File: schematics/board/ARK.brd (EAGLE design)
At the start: 89 x 89 mm, 213 parts, among them IC2 STM32F103C8T, Q5 8MHz

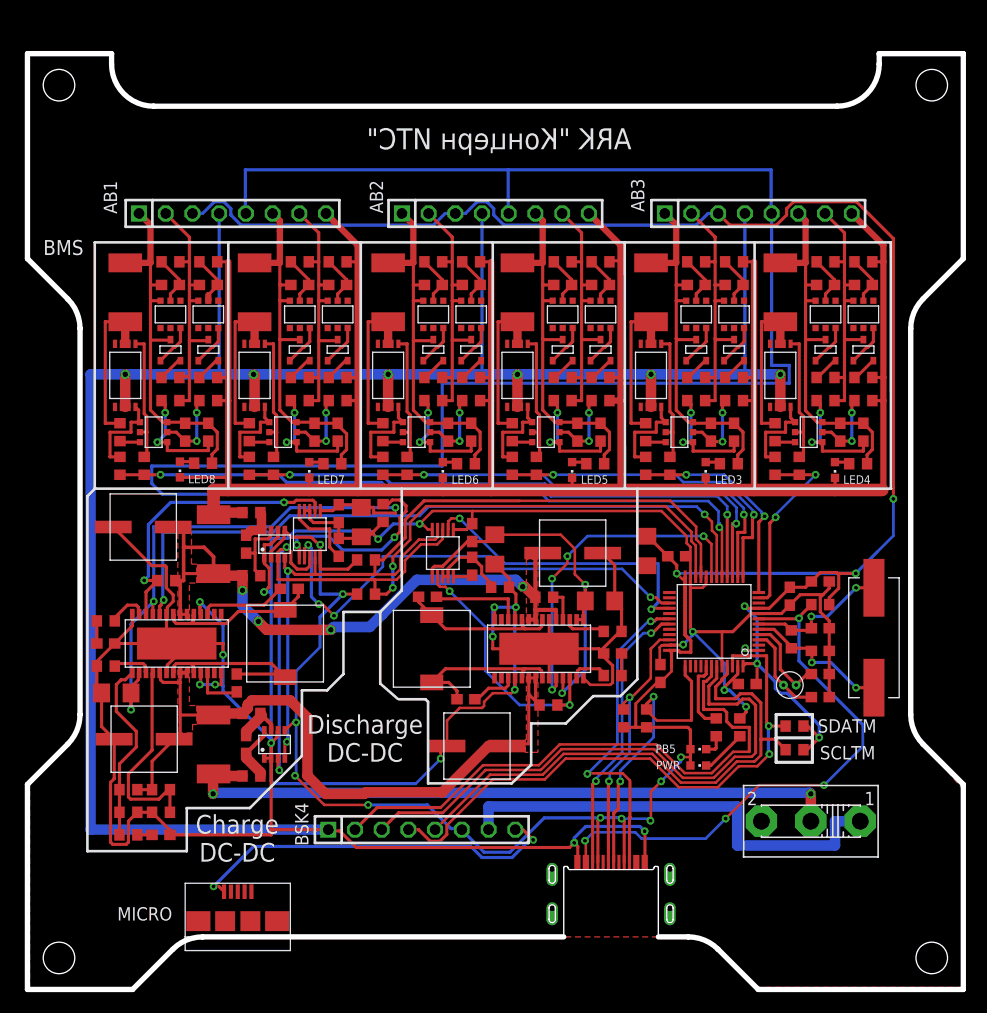
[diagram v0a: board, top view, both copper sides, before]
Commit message: Обновлен список плат, работа над платой ПН
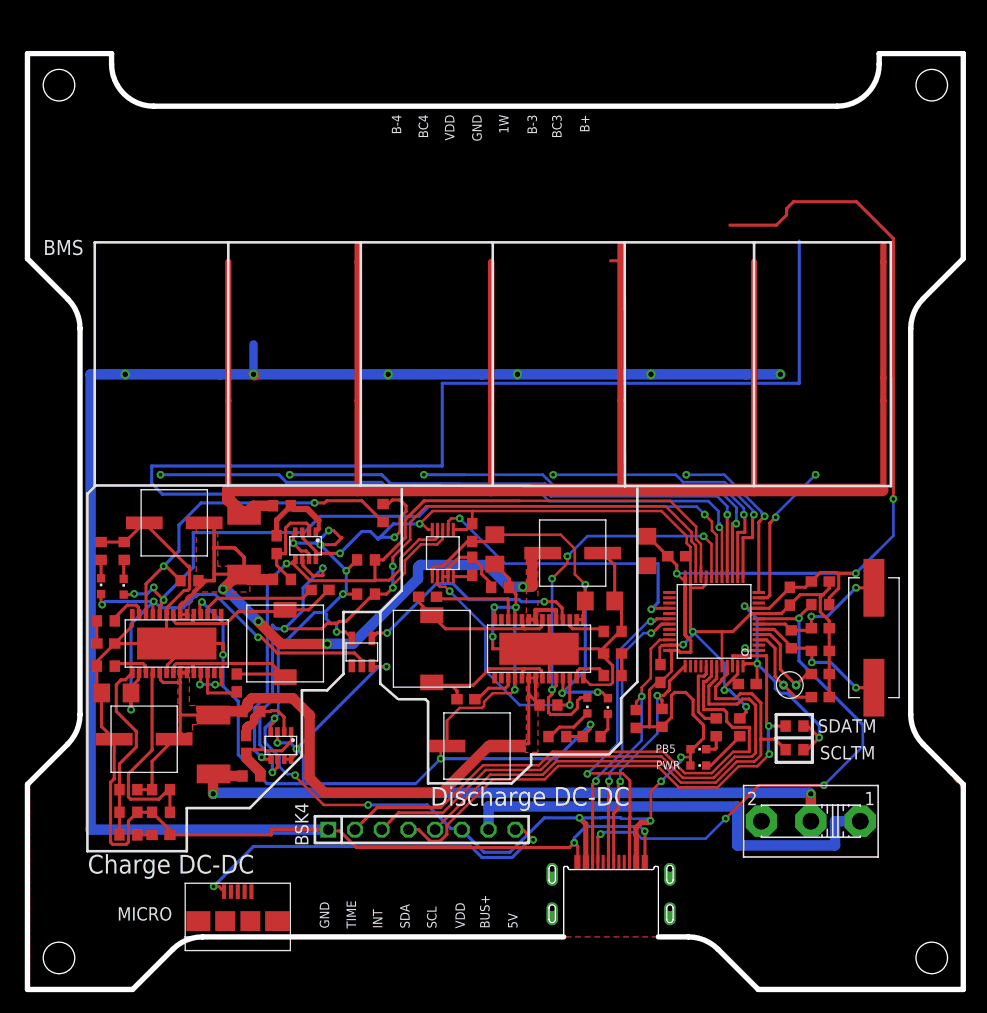
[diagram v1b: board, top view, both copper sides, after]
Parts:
- removed AB1, AB2, AB3: (no value), pinheadCS:1X08
- removed C1, C10, C11, C12, C17, C18, C19, C2, C20, C21, C22, C23, C24, C25, C26, C27, C28, C3, C32, C4, C5, C6, C7, C8, C9: 0,1µ, rcl:C0603
- removed C42: 1µ, rcl:C0603
- removed C43: 10µ, rcl:C1206
- removed LED4, LED5, LED6, LED7: (no value), led:CHIPLED_0603
- removed R1, R17, R33, R41, R49, R80, R83, R84, R85, R86, R9: 2k, resistor:R0603
- removed R10, R11, R18, R19, R2, R3, R34, R35, R42, R43, R50, R51: 330R, resistor:R0603
- removed R12, R13, R14, R15, R20, R21, R22, R23, R36, R37, R38, R39, R4, R44, R45, R46, R47, R5, R52, R53, R54, R55, R6, R7, R88, R89, R90, R91, R92, R93, R94, R95, R96, R97, R98, R99: 100R, resistor:R0603
- removed R16, R24, R40, R48, R56, R8: R05, rcl:R2512
- removed R63: 1M, resistor:R0603
- removed U$1, U$15, U$24, U$25, U$26, U$8: FS8205A-, CanCubeSat:FS8205A-
- removed U$10, U$17, U$3, U$31, U$38, U$45: HY2120, CanCubeSat:HY2120
- removed U$11, U$12, U$18, U$19, U$32, U$33, U$39, U$4, U$40, U$46, U$47, U$5: HY2213, CanCubeSat:HY2213
- removed U$13, U$14, U$20, U$21, U$34, U$35, U$41, U$42, U$48, U$49, U$6, U$7: SI2302CDS, CanCubeSat:SI2302CDS
- removed U$60: AD5272, CanCubeSat:AD5272
- added LED1, LED2: (no value), led:CHIPLED_0603
- added R31, R32, R57: 2k, resistor:R0603
- added U$2: INVERTER, CanCubeSat:INVERTER
- R70: value 14k3 -> 24k3
- R72: value 91k -> 232k
- moved LED3 25.1 mm to (53.2, 27.0)
- moved LED8 13.4 mm to (7.00, 38.4), turned to 0 degrees
- moved R100 12.8 mm to (7.00, 41.7), turned to 270 degrees
- moved C35 2.98 mm to (14.0, 44.4)
- moved R76 2.97 mm to (24.2, 46.0)
- moved U$57 2.95 mm to (26.4, 42.2), turned to 270 degrees
- moved C34 2.92 mm to (27.8, 38.0)
- moved R77 2.92 mm to (24.2, 39.0)
- moved R75 2.90 mm to (20.6, 42.3)
- moved C41 2.90 mm to (23.7, 42.3)
- moved R72 2.20 mm to (15.4, 38.9)
- moved R27 1.45 mm to (60.4, 25.8)
- moved R64 1.20 mm to (57.9, 25.7)
- moved INA219#1 0.61 mm to (24.1, 23.2), turned to 270 degrees
- moved R74 0.20 mm to (21.3, 26.4)
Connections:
- removed net B-1: AB1.6, C1.2, C2.2, C4.2, R8.2, R86.1, U$3.6, U$5.3, U$7.3
- removed net B-2: AB1.1, C25.2, C26.2, C28.2, R100.1, R56.2, U$45.6, U$47.3, U$49.3
- removed net B-3: AB2.6, C5.2, C6.2, C8.2, R16.2, R84.1, U$10.6, U$12.3, U$14.3
- removed net B-4: AB2.1, C21.2, C22.2, C24.2, R48.2, R85.1, U$38.6, U$40.3, U$42.3
- removed net B-5: AB3.6, C10.2, C12.2, C9.2, R24.2, R83.1, U$17.6, U$19.3, U$21.3
- removed net B-6: AB3.1, C17.2, C18.2, C20.2, R40.2, R80.1, U$31.6, U$33.3, U$35.3
- removed net DPC_RST: IC2.27, U$60.7
- removed net N$1: C1.1, R2.1, U$3.5
- removed net N$10: R5.1, U$7.2
- removed net N$100: U$46.6, U$48.1
- removed net N$101: R52.1, U$48.2
- removed net N$102: U$47.6, U$49.1
- removed net N$103: R53.1, U$49.2
- removed net N$104: R49.2, R56.1, U$1.67
- removed net N$107: C26.1, R51.1, U$45.4
- removed net N$108: C28.1, R55.1, U$47.2
- removed net N$110: AB1.2, C27.2, R51.2, R53.2, R55.2, U$46.3, U$48.3
- removed net N$13: R1.2, R8.1, U$26.67
- removed net N$141: C40.2, INA219#1.7, R74.2
- removed net N$15: C2.1, R3.1, U$3.4
- removed net N$154: C42.1, U$60.5
- removed net N$16: C5.1, R10.1, U$10.5
- removed net N$18: R9.1, U$10.3
- removed net N$19: C7.1, R14.1, U$11.2
- removed net N$2: C4.1, R7.1, U$5.2
- removed net N$20: U$11.6, U$13.1
- removed net N$21: R12.1, U$13.2
- removed net N$22: U$12.6, U$14.1
- removed net N$23: R13.1, U$14.2
- removed net N$24: R16.1, R9.2, U$25.67
- removed net N$27: C6.1, R11.1, U$10.4
- removed net N$28: C8.1, R15.1, U$12.2
- removed net N$3: R1.1, U$3.3
- removed net N$30: AB2.7, C7.2, R11.2, R13.2, R15.2, U$11.3, U$13.3
- removed net N$33: C9.1, R18.1, U$17.5
- removed net N$34: R17.1, U$17.3
- removed net N$35: C11.1, R22.1, U$18.2
- removed net N$36: U$18.6, U$20.1
- removed net N$37: R20.1, U$20.2
- removed net N$38: U$19.6, U$21.1
- removed net N$39: R21.1, U$21.2
- removed net N$4: C3.1, R6.1, U$4.2
- removed net N$40: R17.2, R24.1, U$24.67
- removed net N$43: C10.1, R19.1, U$17.4
- removed net N$44: C12.1, R23.1, U$19.2
- removed net N$45: C32.1, C39.1, C43.1, U$59.11, U$59.16, U$60.1
- removed net N$46: AB3.7, C11.2, R19.2, R21.2, R23.2, U$18.3, U$20.3
- removed net N$53: R63.1, U$16.18
- removed net N$57: LED5.A, R84.2
- removed net N$58: LED6.A, R85.2
- removed net N$59: LED7.A, R86.2
- removed net N$6: U$4.6, U$6.1
- removed net N$65: C17.1, R34.1, U$31.5
- removed net N$66: R33.1, U$31.3
- removed net N$67: C19.1, R38.1, U$32.2
- removed net N$68: U$32.6, U$34.1
- removed net N$69: R36.1, U$34.2
- removed net N$7: R4.1, U$6.2
- removed net N$70: U$33.6, U$35.1
- removed net N$71: R37.1, U$35.2
- removed net N$72: R33.2, R40.1, U$15.67
- removed net N$75: C18.1, R35.1, U$31.4
- removed net N$76: C20.1, R39.1, U$33.2
- removed net N$78: AB3.2, C19.2, R35.2, R37.2, R39.2, U$32.3, U$34.3
- removed net N$8: AB1.7, C3.2, R3.2, R5.2, R7.2, U$4.3, U$6.3
- removed net N$81: C21.1, R42.1, U$38.5
- removed net N$82: R41.1, U$38.3
- removed net N$83: C23.1, R46.1, U$39.2
- removed net N$84: U$39.6, U$41.1
- removed net N$85: R44.1, U$41.2
- removed net N$86: U$40.6, U$42.1
- removed net N$87: R45.1, U$42.2
- removed net N$88: R41.2, R48.1, U$8.67
- removed net N$9: U$5.6, U$7.1
- removed net N$91: C22.1, R43.1, U$38.4
- removed net N$92: C24.1, R47.1, U$40.2
- removed net N$94: AB2.2, C23.2, R43.2, R45.2, R47.2, U$39.3, U$41.3
- removed net N$97: C25.1, R50.1, U$45.5
- removed net N$98: R49.1, U$45.3
- removed net N$99: C27.1, R54.1, U$46.2
- removed net OC1: R95.2, U$26.5, U$3.2
- removed net OC2: R99.2, U$1.5, U$45.2
- removed net OC3: R93.2, U$10.2, U$25.5
- removed net OC4: R97.2, U$38.2, U$8.5
- removed net OC5: R91.2, U$17.2, U$24.5
- removed net OC6: R89.2, U$15.5, U$31.2
- removed net OD1: R94.2, U$26.4, U$3.1
- removed net OD2: R98.2, U$1.4, U$45.1
- removed net OD3: R92.2, U$10.1, U$25.4
- removed net OD4: R96.2, U$38.1, U$8.4
- removed net OD5: R90.2, U$17.1, U$24.4
- removed net OD6: R88.2, U$15.4, U$31.1
- new net A: C39.1, LED8.A, U$2.P$2, U$59.11, U$59.16
- new net N$14: C40.2, INA219#1.2, R74.2
- new net Y: U$16.18, U$2.P$4
- net 1W: no longer AB1.5, AB2.5, AB3.5
- net BMS+: no longer AB1.8, AB2.8, AB3.8, LED3.C, LED4.C, LED5.C, LED6.C, LED7.C, LED8.C, R10.2, R12.2, R14.2, R18.2, R2.2, R20.2, R22.2, R34.2, R36.2, R38.2, R4.2, R42.2, R44.2, R46.2, R50.2, R52.2, R54.2, R6.2
- net BMS1: no longer R94.1, R95.1
- net BMS2: no longer R98.1, R99.1
- net BMS3: no longer R92.1, R93.1
- net BMS4: no longer R96.1, R97.1
- net BMS5: no longer R90.1, R91.1
- net BMS6: no longer R88.1, R89.1
- net GND: now also INA219#1.3, INA219#1.7, INA219#1.8, R100.1, R31.1, R32.1, R57.1, R70.2, U$2.P$3, U$57.3, U$57.8; no longer AB1.4, AB2.4, AB3.4, C32.2, C42.2, C43.2, INA219#1.1, INA219#1.2, INA219#1.6, R70.1, U$1.23, U$15.23, U$24.23, U$25.23, U$26.23, U$57.1, U$57.6, U$60.3, U$60.4, U$8.23
- net INA_BMS+: no longer R63.2
- net N$147: now also INA219#1.1; no longer INA219#1.8
- net N$150: now also U$57.1; no longer U$57.8
- net N$151: now also U$57.2; no longer U$57.7
- net N$25: now also R70.1; no longer U$60.2
- net N$26: now also LED1.C, R31.2; no longer R70.2, U$60.6
- net N$47: now also LED1.A
- net N$54: now also LED2.C, R32.2; no longer LED3.A, R80.2
- net N$56: now also LED3.C, R57.2; no longer LED4.A, R83.2
- net N$60: now also LED8.C; no longer LED8.A
- net PGOOD1: now also LED2.A
- net PGOOD2: now also LED3.A
- net SCL: now also INA219#1.5, U$57.5; no longer INA219#1.4, U$57.4, U$60.9
- net SDA: now also INA219#1.6, U$57.6; no longer INA219#1.3, U$57.3, U$60.8
- net VDD: now also INA219#1.4, U$2.P$5, U$57.4, U$57.7; no longer AB1.3, AB2.3, AB3.3, INA219#1.5, U$57.2, U$57.5, U$60.10
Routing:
- net 1W: track 211.9 -> 146.0 mm
- net GND: track 579.7 -> 520.3 mm, vias 25 -> 28
- net N$45: track 55.7 -> 0.00 mm, vias 3 -> 0
- net A: track 0.00 -> 46.0 mm, vias 0 -> 4
- net DPC_RST: track 46.0 -> 0.00 mm, vias 4 -> 0
- net VDD: track 303.0 -> 259.4 mm, vias 17 -> 20
- net BMS+: track 245.9 -> 204.3 mm
- net B-6: track 36.0 -> 0.00 mm
- net B-4: track 35.9 -> 0.00 mm
- net B-2: track 35.8 -> 0.00 mm
- net B-5: track 35.8 -> 0.00 mm
- net B-3: track 35.8 -> 0.00 mm
- net B-1: track 35.7 -> 0.00 mm
- net N$110: track 25.3 -> 0.00 mm
- net N$78: track 25.2 -> 0.00 mm
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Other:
- board text added: "1W"
- board text added: "5V"
- board text added: "B+"
- board text added: "B-3"
- board text added: "B-4"
- board text added: "BC3"
- board text added: "BC4"
- board text added: "BUS+"
- board text added: "GND"
- board text added: "INT"
- board text added: "SCL"
- board text added: "SDA"
- board text added: "TIME"
- board text added: "VDD"

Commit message: Добавлены герберы плат BSK1-4, PL, SP и SPIDER
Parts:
- removed BSK4: (no value), pinheadCS:1X08
- removed C005R: 32,768KHz, CanCubeSat:C005R
- removed C13, C14, C33, C34, C51: 0,1µ, rcl:C0603
- removed C30, C36: 680p, rcl:C0603
- removed C31, C39: 4.7µ, rcl:C1206
- removed C35: 150µ, CanCubeSat:ECAP150
- removed C37: 220µ, CanCubeSat:ECAP220
- removed C38: 3,3n, rcl:C0603
- removed LED1, LED2, LED3, LED8: (no value), led:CHIPLED_0603
- removed MICRO: 629105136821, MicroUSB:629105136821
- removed Q5: 8MHz, 9C-8.000MEEJ-T:XTAL_9C-8.000MEEJ-T
- removed R25, R26: 5k1, resistor:R0603
- removed R29: 150k, resistor:R0603
- removed R31: 2k, resistor:R0603
- removed R61: 91K, resistor:R0603
- removed R62, R72: 232k, resistor:R0603
- removed R70: 24k3, resistor:R0603
- removed R78: 1M, resistor:R0603
- removed R87: 680k, resistor:R0603
- removed S1: (no value), cansat-lib:UNICS-SWITCH
- removed U$16: LTC3119, CanCubeSat:LTC3119
- added C1: 1nF, rcl:C0603
- added C10, C56, C9: 0,1µ, rcl:C0603
- added C2: 10nF, rcl:C0603
- added C3, C57: 10µ, rcl:C1206
- added C4, C5, C6, C7, C8: 100nF, rcl:C0603
- added CAM1, CAM2, SWITCH: (no value), pinheadCS:1X02
- added INVERT: INVERTER., CanCubeSat:SC70
- added JP1: (no value), pinheadCS:2X08
- added LD1117S33: LD1117S33, CanCubeSat:SOT223
- added LED_G1, LED_G2, LED_R1, LED_R2: (no value), led:CHIPLED_0603
- added OPA: OPA333, CanCubeSat:SOT23-5
- added R1: 91K, resistor:R0603
- added R2: 3313J-1-205E, CanCubeSat:TRIM_3313J-1-205E
- added R3: 14K3, resistor:R0603
- added R33: 2k, resistor:R0603
- added R4, R5, R6: 3314G-1-504E, CanCubeSat:TRIM_3314G-1-504E
- added U$1: MF-R400, CanCubeSat:MF-R400
- added U$12: FFC-CONNECT68611, CanCubeSat:68611
- 3,3µH1: value 3,3µ -> 3,3µH
- AD5272#2: device CanCubeSat:AD5272 -> CanCubeSat:MSOP10
- C44: value 27pF -> 680p
- C45: value 27pF -> 4.7µ; device rcl:C0603 -> rcl:C1206
- C46: value 10pF -> 3,3n
- C47: value 10pF -> 150µ; device rcl:C0603 -> CanCubeSat:ECAP150-CMD
- C48, C55: value 100nF -> 220µ; device rcl:C0603 -> CanCubeSat:ECAP220-CMD
- C49: value 150µ -> 0,1µ; device CanCubeSat:ECAP150 -> rcl:C0603
- C50: value 220µ -> 0,1µ; device CanCubeSat:ECAP220 -> rcl:C0603
- C52: value 10µ -> 680p; device rcl:C1206 -> rcl:C0603
- C53: value 100nF -> 4.7µ; device rcl:C0603 -> rcl:C1206
- C54: value 100nF -> 150µ; device rcl:C0603 -> CanCubeSat:ECAP150-CMD
- INA219#1, U$57: device CanCubeSat:INA219AID -> CanCubeSat:SOT23-8
- R30: value 14K3 -> 150k
- U$2: value INVERTER -> Q24; device CanCubeSat:INVERTER -> CanCubeSat:Q24
- U$23: value USB-C -> LTC31191; device CanCubeSat:USB-C -> CanCubeSat:LTC3119+VIA
- U$59: value LTC3119 -> LTC31191; device CanCubeSat:LTC3119 -> CanCubeSat:LTC3119+VIA
- moved C53 64.4 mm to (16.4, 67.0)
- moved R71 63.5 mm to (59.3, 71.3)
- moved C47 60.0 mm to (15.9, 22.5)
- moved R73 59.5 mm to (55.5, 69.0), turned to 180 degrees
- moved C44 59.2 mm to (20.4, 12.5)
- moved R74 58.2 mm to (55.5, 73.6)
- moved U$23 58.1 mm to (24.4, 54.1), turned to 90 degrees
- moved INA219#1 53.4 mm to (50.6, 69.6), turned to 180 degrees
- moved C46 52.6 mm to (24.4, 15.0)
- moved C55 51.6 mm to (15.9, 56.5), turned to 180 degrees
- moved R28 50.2 mm to (15.4, 64.0), turned to 0 degrees
- moved R57 48.8 mm to (7.30, 46.9)
- moved C45 47.5 mm to (32.4, 12.0)
- moved C48 45.5 mm to (32.9, 22.5)
- moved C54 44.0 mm to (32.9, 56.5), turned to 180 degrees
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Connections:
- removed net I2CINT: BSK4.3, IC2.43
- removed net N$11: 3,3µH1.2, C13.1, U$16.21, U$16.24
- removed net N$12: 3,3µH1.1, C14.1, U$16.5, U$16.8
- removed net N$133: C44.1, IC2.6, Q5.1, R78.1
- removed net N$145: C45.1, IC2.5, Q5.2, R78.2
- removed net N$148: C005R.P$2, C47.1, IC2.4
- removed net N$152: C005R.P$1, C46.1, IC2.3
- removed net N$25: R70.1, R72.1, U$59.12
- removed net N$26: LED1.C, R31.2
- removed net N$29: R28.2, U$16.17
- removed net N$32: C13.2, U$16.26
- removed net N$41: R29.1, U$16.13
- removed net N$42: C30.1, R29.2
- removed net N$47: AD5272#2.1, C31.1, C51.1, C52.1, LED1.A, U$16.11, U$16.15, U$16.16
- removed net N$5: AD5272#2.2, R61.1, U$16.12
- removed net N$52: C14.2, U$16.3
- removed net N$54: LED2.C, R32.2
- removed net N$55: R62.2, R87.1, U$59.18
- removed net N$56: LED3.C, R57.2
- removed net N$60: LED8.C, R100.2
- removed net RX-C: IC2.31, U$23.RX0
- removed net TX-C: IC2.30, U$23.TX0
- removed net VDD: BSK4.6, C15.1, C16.1, C48.1, C53.1, C54.1, C55.1, IC2.1, IC2.24, IC2.36, IC2.48, IC2.9, INA219#1.4, PB5.A, PWR.A, R101.1, R102.1, R25.1, R26.1, R27.1, R64.1, R79.1, U$2.P$5, U$23.3V3/BUS0, U$23.3V3/BUS1, U$57.4, U$57.7
- new net 1.65: R4.2, R5.3
- new net 302: OPA.P$4, R5.2
- new net 3V3: C15.1, C16.1, C2.2, C5.1, C6.1, C7.1, C8.1, IC2.1, IC2.24, IC2.36, IC2.48, IC2.9, INA219#1.4, JP1.9, PB5.A, PWR.A, R101.1, R102.1, R27.1, R64.1, R79.1, U$12.P$1, U$12.P$2, U$2.P$4, U$57.4, U$57.7
- new net 3V3-STAB: C3.1, INVERT.P$5, LD1117S33.P$3, OPA.P$5, R4.1
- new net GND-OUT: CAM1.2, CAM2.2, JP1.11, JP1.12, U$1.P$2, U$12.P$3, U$12.P$5, U$12.P$7, U$12.P$9
- new net N$1: C1.1, IC2.5
- new net N$215: AD5272#2.1, C53.1, C56.1, C57.1, LED_G2.A, U$23.11, U$23.15, U$23.16
- new net N$234: C45.1, LED_G1.A, U$59.11, U$59.16
- new net N$3: AD5272#2.2, R1.2, U$23.12
- new net N$4: C1.2, U$2.P$3
- new net N$77: 3,3µH1.2, C49.1, U$23.21, U$23.24
- new net N$78: 3,3µH1.1, C50.1, U$23.5, U$23.8
- new net N$79: R28.2, U$23.17
- new net N$80: C49.2, U$23.26
- new net N$81: R30.1, U$23.13
- new net N$82: C52.1, R30.2
- new net N$84: C50.2, U$23.3
- new net N$85: LED_R1.A, R32.2
- new net N$87: LED_R2.A, R57.2
- new net N$89: R6.2, U$59.12
- new net N$91: LED_G1.C, R100.2
- new net N$92: LED_G2.C, R33.2
- new net RUN: OPA.P$3, R2.2
- new net RX-S: IC2.31, U$12.P$4
- new net TX-S: IC2.30, U$12.P$6
- net 1W: now also JP1.7
- net 5V: now also CAM1.1, CAM2.1, JP1.10; no longer BSK4.8, MICRO.5V
- net A: now also INVERT.P$2, OPA.P$1, R32.1, R5.1, U$59.18; no longer C39.1, LED8.A, U$2.P$2, U$59.11, U$59.16
- net BMS+: now also C4.1, JP1.8, LD1117S33.P$4
- net BMS1: now also IC2.16, JP1.1; no longer IC2.15
- net BMS2: now also IC2.15, JP1.2; no longer IC2.16
- net BMS3: now also IC2.14, JP1.3; no longer IC2.13
- net BMS4: now also IC2.13, JP1.4; no longer IC2.14
- net BMS5: now also IC2.12, JP1.5; no longer IC2.11
- net BMS6: now also IC2.11, JP1.6; no longer IC2.12
- net BUS+: now also SWITCH.2; no longer S1.2
- net BUSPLUS: now also JP1.16, SWITCH.1; no longer BSK4.7, S1.1
- net GND: now also C2.1, C3.2, C4.2, C47.P$2, C48.P$2, C5.2, C54.P$2, C55.P$2, C56.2, C57.2, C6.2, C7.2, C8.2, INVERT.P$3, LD1117S33.P$2, OPA.P$2, R2.3, R3.2, R33.1, R4.3, R6.3, U$1.P$1, U$2.P$2, U$23.14, U$23.20, U$23.25, U$23.28, U$23.29, U$23.4, U$23.9, U$23.P$1, U$23.P$10, U$23.P$2, U$23.P$3, U$23.P$4, U$23.P$5, U$23.P$6, U$23.P$7, U$23.P$8, U$23.P$9, U$59.P$1, U$59.P$10, U$59.P$2, U$59.P$3, U$59.P$4, U$59.P$5, U$59.P$6, U$59.P$7, U$59.P$8, U$59.P$9; no longer BSK4.1, C30.2, C31.2, C35.P$2, C36.2, C37.P$2, C38.2, C39.2, C47.2, C48.2, C49.P$2, C50.P$2, C51.2, C54.2, C55.2, MICRO.GND, MICRO.Z1, MICRO.Z2, MICRO.Z3, MICRO.Z4, R30.2, R31.1, R32.1, R57.1, R62.1, R70.2, U$16.14, U$16.20, U$16.25, U$16.28, U$16.29, U$16.4, U$16.9, U$2.P$3, U$23.GND0, U$23.GND1
- net INA_BMS+: now also C47.P$1, C55.P$1, R6.1, U$23.19, U$23.22, U$23.23; no longer C35.P$1, C50.P$1, R72.2, U$16.19, U$16.22, U$16.23
- net INA_BUS+: now also C48.P$1, C54.P$1, R1.1, R2.1, U$23.6, U$23.7; no longer C37.P$1, C49.P$1, R61.2, R87.2, U$16.6, U$16.7
- net N$129: now also C41.2; no longer C34.2
- net N$131: now also C40.1; no longer C33.1
- net N$132: now also C41.1; no longer C34.1
- net N$136: now also C44.1; no longer C36.1
- net N$139: now also C46.1; no longer C38.1
- net N$14: now also C9.2; no longer C40.2
- net N$144: now also C40.2; no longer C33.2
- net N$147: now also C9.1; no longer C40.1
- net N$150: now also C10.1; no longer C41.1
- net N$151: now also C10.2; no longer C41.2
- net N$48: now also R3.1; no longer R30.1
- net NRST: now also U$12.P$11; no longer U$23.NRST/EN
- net PGOOD1: now also IC2.19, LED_R1.C; no longer IC2.18, LED2.A
- net PGOOD2: now also IC2.18, LED_R2.C, U$23.10; no longer IC2.19, LED3.A, U$16.10
- net SCLTM: now also JP1.13; no longer BSK4.5, R25.2
- net SDATM: now also JP1.14; no longer BSK4.4, R26.2
- net SWC: now also U$12.P$10; no longer U$23.SWC/TXD
- net SWD: now also U$12.P$8; no longer U$23.SWD/RXD
- net TIME: now also JP1.15; no longer BSK4.2
- net Y: now also INVERT.P$4, R57.1, U$23.18; no longer U$16.18, U$2.P$4
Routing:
- net VDD: track 259.4 -> 0.00 mm, vias 20 -> 0
- net GND: track 520.3 -> 261.9 mm, vias 28 -> 21
- net 3V3: track 0.00 -> 194.2 mm, vias 0 -> 19
- net GND-OUT: track 0.00 -> 165.9 mm
- net BMS+: track 204.3 -> 88.6 mm
- net 1W: track 146.0 -> 55.1 mm, vias 1 -> 3
- net INA_BUS+: track 71.9 -> 131.1 mm, vias 0 -> 3
- net I2CINT: track 53.6 -> 0.00 mm
- net BUS+: track 64.3 -> 12.5 mm, vias 2 -> 1
- net INA_BMS+: track 74.2 -> 121.2 mm
- net 5V: track 36.4 -> 81.1 mm, vias 2 -> 0
- net 3V3-STAB: track 0.00 -> 44.1 mm
- net BMS6: track 16.6 -> 59.9 mm, vias 2 -> 1
- net BMS5: track 14.4 -> 56.5 mm, vias 2 -> 1
- net RX-S: track 0.00 -> 41.7 mm, vias 0 -> 2
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- added copper zone on layer 1, net BMS+
- added copper zone on layer 1, net BUSPLUS
- added copper zone on layer 16, net GND
- added copper zone on layer 16, net GND-OUT
- added copper zone on layer 16, net INA_BMS+
- added copper zone on layer 16, net INA_BUS+
- added copper zone on layer 1, net N$131
- added copper zone on layer 1, net N$132
- added copper zone on layer 1, net N$215
- added copper zone on layer 1, net N$234
- added copper zone on layer 1, net N$77
- added copper zone on layer 1, net N$78
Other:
- board size 89 x 89 mm -> 82 x 92 mm
- board text added: "BMS+"
- board text added: "LTC3119"
- board text removed: "1W"
- board text removed: "5V"
- board text removed: "ARK "Концерн ИТС""
- board text removed: "B+"
- board text removed: "B-3"
- board text removed: "B-4"
- board text removed: "BC3"
- board text removed: "BC4"
- board text removed: "BMS"
- board text removed: "BUS+"
- board text removed: "Charge DC-DC"
- board text removed: "Discharge DC-DC"
- board text removed: "GND"
- board text removed: "INT"
- board text removed: "OFF"
- board text removed: "ON"
- board text removed: "SCL"
- board text removed: "SCLTM"
- board text removed: "SDA"
- board text removed: "SDATM"
- board text removed: "TIME"
- board text removed: "VDD"

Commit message: Исправления АРКа
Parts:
- removed C4: 100nF, rcl:C0603
- removed LD1117S33: LD1117S33, CanCubeSat:SOT223
- added R7: 680k, resistor:R0603
- added U$6: REF3033, CanCubeSat:SOT23-3
- C3: value 10µ -> 470nF; device rcl:C1206 -> rcl:C0603
- R4: value 3314G-1-504E -> 120k; device CanCubeSat:TRIM_3314G-1-504E -> resistor:R0603
- R5: value 3314G-1-504E -> 430k; device CanCubeSat:TRIM_3314G-1-504E -> resistor:R0603
- moved R57 27.2 mm to (9.40, 19.8)
- moved R32 27.0 mm to (7.30, 46.9)
- moved LED_R2 22.4 mm to (9.40, 22.2)
- moved LED_R1 22.4 mm to (7.20, 44.5)
- moved R5 14.1 mm to (4.30, 26.6), turned to 0 degrees
- moved C3 9.27 mm to (5.50, 54.4), turned to 180 degrees
- moved R4 2.11 mm to (4.30, 24.2), turned to 0 degrees
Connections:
- removed net 1.65: R4.2, R5.3
- removed net 302: OPA.P$4, R5.2
- new net N$2: OPA.P$3, R4.2, R5.2, R7.2
- net 3V3: no longer IC2.9
- net 3V3-STAB: now also IC2.9, U$6.2; no longer C3.1, LD1117S33.P$3
- net 5V: now also C3.2, U$6.1
- net A: now also R7.1, U$23.18; no longer R5.1, U$59.18
- net BMS+: no longer C4.1, LD1117S33.P$4
- net GND: now also C3.1, R5.1, U$6.3; no longer C3.2, C4.2, LD1117S33.P$2, R4.3
- net PGOOD1: now also LED_R2.C; no longer LED_R1.C
- net PGOOD2: now also LED_R1.C; no longer LED_R2.C
- net RUN: now also OPA.P$4; no longer OPA.P$3
- net Y: now also U$59.18; no longer U$23.18
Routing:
- net 5V: track 81.1 -> 167.7 mm
- net BMS+: track 88.6 -> 41.7 mm
- net N$2: track 0.00 -> 13.6 mm
- net 1.65: track 13.4 -> 0.00 mm
- net 3V3: track 194.2 -> 181.5 mm, vias 19 -> 17
- net GND: track 261.9 -> 254.5 mm, vias 21 -> 19
- net 302: track 4.92 -> 0.00 mm
- net Y: track 46.1 -> 42.2 mm, vias 6 -> 5
- net 3V3-STAB: track 44.1 -> 47.0 mm
- net PGOOD1: track 78.3 -> 76.3 mm
- net A: track 56.1 -> 57.8 mm
